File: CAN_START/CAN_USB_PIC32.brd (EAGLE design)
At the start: 100 x 80 mm, 3 parts

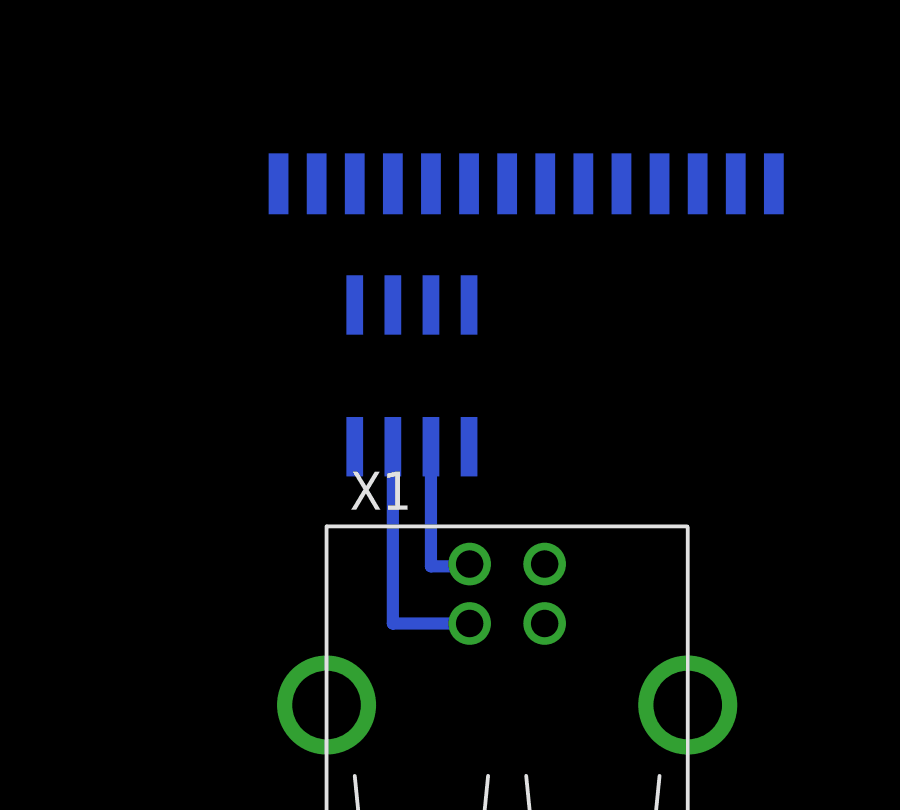
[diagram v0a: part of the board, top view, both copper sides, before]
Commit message: 
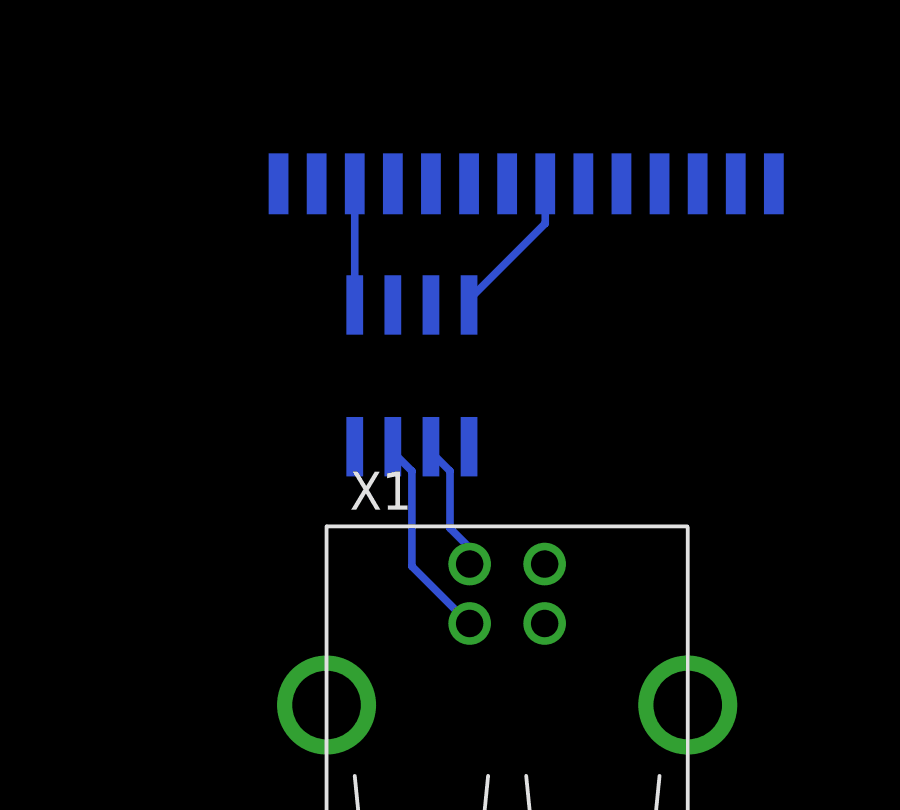
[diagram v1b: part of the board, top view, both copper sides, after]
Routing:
- net N$4: track 0.00 -> 5.09 mm
- net N$3: track 0.00 -> 4.04 mm
- net N$1: track 8.45 -> 6.96 mm
- net N$2: track 5.35 -> 4.44 mm, vias 1 -> 0
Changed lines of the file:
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@@
 <autorouter>
 <pass name="Default">
-<param name="RoutingGrid" value="50mil"/>
+<param name="RoutingGrid" value="25mil"/>
 <param name="tpViaShape" value="round"/>
-<param name="PrefDir.1" value="|"/>
+<param name="PrefDir.1" value="-"/>
 <param name="PrefDir.2" value="0"/>
 <param name="PrefDir.3" value="0"/>
@@
 <param name="PrefDir.14" value="0"/>
 <param name="PrefDir.15" value="0"/>
-<param name="PrefDir.16" value="-"/>
+<param name="PrefDir.16" value="|"/>
 <param name="cfVia" value="8"/>
-<param name="cfNonPref" value="5"/>
+<param name="cfNonPref" value="50"/>
 <param name="cfChangeDir" value="2"/>
 <param name="cfOrthStep" value="2"/>
@@
 <param name="cfAvoid" value="4"/>
 <param name="cfPolygon" value="10"/>
-<param name="cfBase.1" value="0"/>
+<param name="cfBase.1" value="35"/>
 <param name="cfBase.2" value="1"/>
 <param name="cfBase.3" value="1"/>
@@
 </pass>
 <pass name="Follow-me" refer="Default" active="yes">
+<param name="cfNonPref" value="5"/>
+<param name="cfBase.1" value="0"/>
 </pass>
 <pass name="Busses" refer="Default" active="yes">
@@
 <param name="cfBusImpact" value="4"/>
 <param name="cfHugging" value="0"/>
+<param name="cfBase.1" value="30"/>
 <param name="mnVias" value="0"/>
 </pass>
@@
 <pass name="Optimize1" refer="Default" active="yes">
 <param name="cfVia" value="99"/>
+<param name="cfNonPref" value="99"/>
 <param name="cfExtdStep" value="10"/>
 <param name="cfHugging" value="1"/>
+<param name="cfBase.1" value="40"/>
 <param name="mnExtdSteps" value="1"/>
 <param name="mnRipupLevel" value="0"/>
 </pass>
 <pass name="Optimize2" refer="Optimize1" active="yes">
-<param name="cfNonPref" value="0"/>
 <param name="cfChangeDir" value="6"/>
 <param name="cfExtdStep" value="0"/>
@@
 <param name="cfSmdImpact" value="2"/>
 <param name="cfHugging" value="0"/>
+<param name="cfBase.1" value="45"/>
 </pass>
 <pass name="Optimize3" refer="Optimize2" active="yes">
+<param name="cfNonPref" value="90"/>
 <param name="cfChangeDir" value="8"/>
 <param name="cfPadImpact" value="0"/>
 <param name="cfSmdImpact" value="0"/>
+<param name="cfBase.1" value="99"/>
 </pass>
 <pass name="Optimize4" refer="Optimize3" active="yes">
-<param name="cfChangeDir" value="25"/>
+<param name="cfChangeDir" value="10"/>
 </pass>
 </autorouter>
@@
 <contactref element="U$1" pad="7"/>
 <contactref element="X1" pad="D+"/>
-<wire x1="33.04" y1="11.43" x2="30.48" y2="11.43" width="0.4064" layer="16"/>
-<wire x1="30.48" y1="11.43" x2="30.48" y2="17.3228" width="0.4064" layer="16"/>
+<wire x1="31.115" y1="16.51" x2="30.48" y2="17.145" width="0.254" layer="16"/>
+<wire x1="31.115" y1="13.335" x2="31.115" y2="16.51" width="0.254" layer="16"/>
+<wire x1="33.02" y1="11.43" x2="31.115" y2="13.335" width="0.254" layer="16"/>
+<wire x1="30.48" y1="17.145" x2="30.48" y2="17.3228" width="0.254" layer="16"/>
+<wire x1="33.02" y1="11.43" x2="33.04" y2="11.43" width="0.254" layer="16"/>
 </signal>
 <signal name="N$2">
 <contactref element="X1" pad="D-"/>
 <contactref element="U$1" pad="6"/>
-<wire x1="33.02" y1="13.335" x2="33.04" y2="13.335" width="0.4064" layer="1"/>
-<wire x1="33.04" y1="13.335" x2="33.04" y2="13.4112" width="0.4064" layer="1"/>
-<via x="33.02" y="13.335" extent="1-16" drill="0.6" shape="square"/>
-<wire x1="31.75" y1="17.3228" x2="31.75" y2="13.335" width="0.4064" layer="16"/>
-<wire x1="31.75" y1="13.335" x2="33.02" y2="13.335" width="0.4064" layer="16"/>
+<wire x1="32.385" y1="16.51" x2="31.75" y2="17.145" width="0.254" layer="16"/>
+<wire x1="32.385" y1="14.605" x2="32.385" y2="16.51" width="0.254" layer="16"/>
+<wire x1="33.02" y1="13.97" x2="32.385" y2="14.605" width="0.254" layer="16"/>
+<wire x1="31.75" y1="17.145" x2="31.75" y2="17.3228" width="0.254" layer="16"/>
+<wire x1="33.02" y1="13.97" x2="33.04" y2="13.4112" width="0.254" layer="16"/>
 </signal>
 <signal name="N$3">
 <contactref element="U$2" pad="26"/>
 <contactref element="U$1" pad="1"/>
-<wire x1="29.21" y1="26.0858" x2="29.21" y2="22.0472" width="0" layer="19" extent="1-1"/>
+<wire x1="29.21" y1="26.0858" x2="29.21" y2="22.0472" width="0.254" layer="16"/>
 </signal>
 <signal name="N$4">
 <contactref element="U$1" pad="4"/>
 <contactref element="U$2" pad="21"/>
-<wire x1="35.56" y1="26.0858" x2="33.02" y2="22.0472" width="0" layer="19" extent="1-1"/>
+<wire x1="35.56" y1="24.765" x2="33.02" y2="22.225" width="0.254" layer="16"/>
+<wire x1="35.56" y1="26.0858" x2="35.56" y2="24.765" width="0.254" layer="16"/>
+<wire x1="33.02" y1="22.225" x2="33.02" y2="22.0472" width="0.254" layer="16"/>
 </signal>
 </signals>
